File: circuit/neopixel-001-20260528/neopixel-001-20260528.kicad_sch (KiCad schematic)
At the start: 67 parts, among them J1 Conn_NeoPixel, J2 Conn_01x02_Pin, J3 Conn_01x02_Pin, P1 ESP32C3_{1}, P10 unitV3, P11 unitV4, P12 unitV4, P2 ESP32C3_{1}, P3 ESP32C3_{2}, P4 ESP32C3_{2}, P5 unitV1, P6 unitV1, P7 unitV2, P8 unitV2, P9 unitV3, SW1 SW_SPST_LED, SW2 SW_SPST_LED, SW3 SW_SPST_LED, SW4 SW_SPST_LED, U1 SSD1306, U2 Aexit_0-50_Voltmeter

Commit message: Update NeoPixel基板の回路図DRをした
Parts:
- J1: footprint Connector_FFC-FPC:JUSHUO_AFA07-S12FCA-00_1x12-1MP_P1.0mm_Horizontal -> (none)
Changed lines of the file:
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@@
 			)
 		)
-		(property "Footprint" "Connector_FFC-FPC:JUSHUO_AFA07-S12FCA-00_1x12-1MP_P1.0mm_Horizontal"
+		(property "Footprint" ""
 			(at 177.8 138.43 0)
 			(hide yes)

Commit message: Update ネオピクセル基板のフットプリント割り当てを進めた
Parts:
- J1: footprint (none) -> @Thrive_footprint_neopixel:AFC01-S12FCA-00
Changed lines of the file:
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@@
 			)
 		)
-		(property "Footprint" ""
+		(property "Footprint" "@Thrive_footprint_neopixel:AFC01-S12FCA-00"
 			(at 177.8 138.43 0)
 			(hide yes)

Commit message: Update ネオピク基板のPCBを進めてる。差動をどう配線すればいいんや
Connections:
- net P4_RX2-: now reaches P7.A10 (RX2-), P8.A10 (RX2-)
- net P4_RX2+: now reaches P7.A11 (RX2+), P8.A11 (RX2+)
- net P4_TX1+: now reaches P7.A2 (TX1+), P8.A2 (TX1+)
- net P4_TX1-: now reaches P7.A3 (TX1-), P8.A3 (TX1-)
- net P4_VBUS: now reaches P7.A4 (VBUS), P7.A9 (VBUS), P7.B4 (VBUS), P7.B9 (VBUS), P8.A4 (VBUS), P8.A9 (VBUS), P8.B4 (VBUS), P8.B9 (VBUS)
- net P4_CC: now reaches P7.A5 (CC), P8.A5 (CC)
- net P4_D-: now reaches P7.A6 (D+), P8.A6 (D+)
- net P4_D+: now reaches P7.A7 (D-), P8.A7 (D-)
- net P4_SBU1: now reaches P7.A8 (SBU1), P8.A8 (SBU1)
- net P4_RX1-: now reaches P7.B10 (RX1-), P8.B10 (RX1-)
- net P4_RX1+: now reaches P7.B11 (RX1+), P8.B11 (RX1+)
- net P4_TX2+: now reaches P7.B2 (TX2+), P8.B2 (TX2+)
- net P4_TX2-: now reaches P7.B3 (TX2-), P8.B3 (TX2-)
- net P4_VCONN: now reaches P7.B5 (VCONN), P8.B5 (VCONN)
- net P4_SBU2: now reaches P7.B8 (SBU2), P8.B8 (SBU2)
- net P6_RX2-: now reaches P11.A10 (RX2-), P12.A10 (RX2-)
- net P6_RX2+: now reaches P11.A11 (RX2+), P12.A11 (RX2+)
- net P6_TX1+: now reaches P11.A2 (TX1+), P12.A2 (TX1+)
- net P6_TX1-: now reaches P11.A3 (TX1-), P12.A3 (TX1-)
- net P6_VBUS: now reaches P11.A4 (VBUS), P11.A9 (VBUS), P11.B4 (VBUS), P11.B9 (VBUS), P12.A4 (VBUS), P12.A9 (VBUS), P12.B4 (VBUS), P12.B9 (VBUS)
- net P6_CC: now reaches P11.A5 (CC), P12.A5 (CC)
- net P6_D-: now reaches P11.A6 (D+), P12.A6 (D+)
- net P6_D+: now reaches P11.A7 (D-), P12.A7 (D-)
- net P6_SBU1: now reaches P11.A8 (SBU1), P12.A8 (SBU1)
- net P6_RX1-: now reaches P11.B10 (RX1-), P12.B10 (RX1-)
- net P6_RX1+: now reaches P11.B11 (RX1+), P12.B11 (RX1+)
- net P6_TX2+: now reaches P11.B2 (TX2+), P12.B2 (TX2+)
- net P6_TX2-: now reaches P11.B3 (TX2-), P12.B3 (TX2-)
- net P6_VCONN: now reaches P11.B5 (VCONN), P12.B5 (VCONN)
- net P6_SBU2: now reaches P11.B8 (SBU2), P12.B8 (SBU2)
- net P1_RX2-: now reaches P1.A10 (RX2-), P2.A10 (RX2-)
- net P1_RX2+: now reaches P1.A11 (RX2+), P2.A11 (RX2+)
- net P1_TX1+: now reaches P1.A2 (TX1+), P2.A2 (TX1+)
- net P1_TX1-: now reaches P1.A3 (TX1-), P2.A3 (TX1-)
- net P1_VBUS: now reaches P1.A4 (VBUS), P1.A9 (VBUS), P1.B4 (VBUS), P1.B9 (VBUS), P2.A4 (VBUS), P2.A9 (VBUS), P2.B4 (VBUS), P2.B9 (VBUS)
- net P1_CC: now reaches P1.A5 (CC), P2.A5 (CC)
- net P1_D-: now reaches P1.A6 (D+), P2.A6 (D+)
- net P1_D+: now reaches P1.A7 (D-), P2.A7 (D-)
- net P1_SBU1: now reaches P1.A8 (SBU1), P2.A8 (SBU1)
- net P1_RX1-: now reaches P1.B10 (RX1-), P2.B10 (RX1-)
- net P1_RX1+: now reaches P1.B11 (RX1+), P2.B11 (RX1+)
- net P1_TX2+: now reaches P1.B2 (TX2+), P2.B2 (TX2+)
- net P1_TX2-: now reaches P1.B3 (TX2-), P2.B3 (TX2-)
- net P1_VCONN: now reaches P1.B5 (VCONN), P2.B5 (VCONN)
- net P1_SBU2: now reaches P1.B8 (SBU2), P2.B8 (SBU2)
- net P3_RX2-: now reaches P5.A10 (RX2-), P6.A10 (RX2-)
- net P3_RX2+: now reaches P5.A11 (RX2+), P6.A11 (RX2+)
- net P3_TX1+: now reaches P5.A2 (TX1+), P6.A2 (TX1+)
- net P3_TX1-: now reaches P5.A3 (TX1-), P6.A3 (TX1-)
- net P3_VBUS: now reaches P5.A4 (VBUS), P5.A9 (VBUS), P5.B4 (VBUS), P5.B9 (VBUS), P6.A4 (VBUS), P6.A9 (VBUS), P6.B4 (VBUS), P6.B9 (VBUS)
- net P3_CC: now reaches P5.A5 (CC), P6.A5 (CC)
- net P3_D-: now reaches P5.A6 (D+), P6.A6 (D+)
- net P3_D+: now reaches P5.A7 (D-), P6.A7 (D-)
- net P3_SBU1: now reaches P5.A8 (SBU1), P6.A8 (SBU1)
- net P3_RX1-: now reaches P5.B10 (RX1-), P6.B10 (RX1-)
- net P3_RX1+: now reaches P5.B11 (RX1+), P6.B11 (RX1+)
- net P3_TX2+: now reaches P5.B2 (TX2+), P6.B2 (TX2+)
- net P3_TX2-: now reaches P5.B3 (TX2-), P6.B3 (TX2-)
- net P3_VCONN: now reaches P5.B5 (VCONN), P6.B5 (VCONN)
- net P3_SBU2: now reaches P5.B8 (SBU2), P6.B8 (SBU2)
- net P2_RX2-: now reaches P3.A10 (RX2-), P4.A10 (RX2-)
- net P2_RX2+: now reaches P3.A11 (RX2+), P4.A11 (RX2+)
- net P2_TX1+: now reaches P3.A2 (TX1+), P4.A2 (TX1+)
- net P2_TX1-: now reaches P3.A3 (TX1-), P4.A3 (TX1-)
- net P2_VBUS: now reaches P3.A4 (VBUS), P3.A9 (VBUS), P3.B4 (VBUS), P3.B9 (VBUS), P4.A4 (VBUS), P4.A9 (VBUS), P4.B4 (VBUS), P4.B9 (VBUS)
- net P2_CC: now reaches P3.A5 (CC), P4.A5 (CC)
- net P2_D-: now reaches P3.A6 (D+), P4.A6 (D+)
- net P2_D+: now reaches P3.A7 (D-), P4.A7 (D-)
- net P2_SBU1: now reaches P3.A8 (SBU1), P4.A8 (SBU1)
- net P2_RX1-: now reaches P3.B10 (RX1-), P4.B10 (RX1-)
- net P2_RX1+: now reaches P3.B11 (RX1+), P4.B11 (RX1+)
- net P2_TX2+: now reaches P3.B2 (TX2+), P4.B2 (TX2+)
- net P2_TX2-: now reaches P3.B3 (TX2-), P4.B3 (TX2-)
- net P2_VCONN: now reaches P3.B5 (VCONN), P4.B5 (VCONN)
- net P2_SBU2: now reaches P3.B8 (SBU2), P4.B8 (SBU2)
- net P5_RX2-: now reaches P10.A10 (RX2-), P9.A10 (RX2-)
- net P5_RX2+: now reaches P10.A11 (RX2+), P9.A11 (RX2+)
- net P5_TX1+: now reaches P10.A2 (TX1+), P9.A2 (TX1+)
- net P5_TX1-: now reaches P10.A3 (TX1-), P9.A3 (TX1-)
- net P5_VBUS: now reaches P10.A4 (VBUS), P10.A9 (VBUS), P10.B4 (VBUS), P10.B9 (VBUS), P9.A4 (VBUS), P9.A9 (VBUS), P9.B4 (VBUS), P9.B9 (VBUS)
- net P5_CC: now reaches P10.A5 (CC), P9.A5 (CC)
- net P5_D-: now reaches P10.A6 (D+), P9.A6 (D+)
- net P5_D+: now reaches P10.A7 (D-), P9.A7 (D-)
- net P5_SBU1: now reaches P10.A8 (SBU1), P9.A8 (SBU1)
- net P5_RX1-: now reaches P10.B10 (RX1-), P9.B10 (RX1-)
- net P5_RX1+: now reaches P10.B11 (RX1+), P9.B11 (RX1+)
- net P5_TX2+: now reaches P10.B2 (TX2+), P9.B2 (TX2+)
- net P5_TX2-: now reaches P10.B3 (TX2-), P9.B3 (TX2-)
- net P5_VCONN: now reaches P10.B5 (VCONN), P9.B5 (VCONN)
- net P5_SBU2: now reaches P10.B8 (SBU2), P9.B8 (SBU2)
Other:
- moved on the sheet: C1, C10, C11, C12, C13, C14, C15, C16, C17, C18, C19, C2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

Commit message: Update ネオピクセル基板のコンポーネントコンポーネント再度仮配置。時間返せ
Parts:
- P10, P12, P2, P4, P6, P8: footprint @Thrive_footprint_neopixel:USB_Type-C_Vertical_ C6332304 -> Connector_USB:USB_C_Receptacle_GCT_USB4105-xx-A_16P_TopMnt_Horizontal
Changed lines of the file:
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@@
 			)
 		)
-		(property "Footprint" "@Thrive_footprint_neopixel:USB_Type-C_Vertical_ C6332304"
+		(property "Footprint" "Connector_USB:USB_C_Receptacle_GCT_USB4105-xx-A_16P_TopMnt_Horizontal"
 			(at 191.77 142.24 0)
 			(hide yes)
@@
 			)
 		)
-		(property "Footprint" "@Thrive_footprint_neopixel:USB_Type-C_Vertical_ C6332304"
+		(property "Footprint" "Connector_USB:USB_C_Receptacle_GCT_USB4105-xx-A_16P_TopMnt_Horizontal"
 			(at 92.71 142.24 0)
 			(hide yes)
@@
 			)
 		)
-		(property "Footprint" "@Thrive_footprint_neopixel:USB_Type-C_Vertical_ C6332304"
+		(property "Footprint" "Connector_USB:USB_C_Receptacle_GCT_USB4105-xx-A_16P_TopMnt_Horizontal"
 			(at 191.77 232.41 0)
 			(hide yes)
@@
 			)
 		)
-		(property "Footprint" "@Thrive_footprint_neopixel:USB_Type-C_Vertical_ C6332304"
+		(property "Footprint" "Connector_USB:USB_C_Receptacle_GCT_USB4105-xx-A_16P_TopMnt_Horizontal"
 			(at 92.71 232.41 0)
 			(hide yes)
@@
 			)
 		)
-		(property "Footprint" "@Thrive_footprint_neopixel:USB_Type-C_Vertical_ C6332304"
+		(property "Footprint" "Connector_USB:USB_C_Receptacle_GCT_USB4105-xx-A_16P_TopMnt_Horizontal"
 			(at 92.71 52.07 0)
 			(hide yes)
@@
 			)
 		)
-		(property "Footprint" "@Thrive_footprint_neopixel:USB_Type-C_Vertical_ C6332304"
+		(property "Footprint" "Connector_USB:USB_C_Receptacle_GCT_USB4105-xx-A_16P_TopMnt_Horizontal"
 			(at 191.77 52.07 0)
 			(hide yes)

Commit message: Update ネオピクセル基板のコンポーネントを再配置した。明日配線する。もう今日か
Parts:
- P10, P12, P2, P4, P6, P8: footprint Connector_USB:USB_C_Receptacle_GCT_USB4105-xx-A_16P_TopMnt_Horizontal -> @Thrive_footprint_neopixel:USB_Type-C_Vertical_ C6332304
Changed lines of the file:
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@@
 			)
 		)
-		(property "Footprint" "Connector_USB:USB_C_Receptacle_GCT_USB4105-xx-A_16P_TopMnt_Horizontal"
+		(property "Footprint" "@Thrive_footprint_neopixel:USB_Type-C_Vertical_ C6332304"
 			(at 191.77 142.24 0)
 			(hide yes)
@@
 			)
 		)
-		(property "Footprint" "Connector_USB:USB_C_Receptacle_GCT_USB4105-xx-A_16P_TopMnt_Horizontal"
+		(property "Footprint" "@Thrive_footprint_neopixel:USB_Type-C_Vertical_ C6332304"
 			(at 92.71 142.24 0)
 			(hide yes)
@@
 			)
 		)
-		(property "Footprint" "Connector_USB:USB_C_Receptacle_GCT_USB4105-xx-A_16P_TopMnt_Horizontal"
+		(property "Footprint" "@Thrive_footprint_neopixel:USB_Type-C_Vertical_ C6332304"
 			(at 191.77 232.41 0)
 			(hide yes)
@@
 			)
 		)
-		(property "Footprint" "Connector_USB:USB_C_Receptacle_GCT_USB4105-xx-A_16P_TopMnt_Horizontal"
+		(property "Footprint" "@Thrive_footprint_neopixel:USB_Type-C_Vertical_ C6332304"
 			(at 92.71 232.41 0)
 			(hide yes)
@@
 			)
 		)
-		(property "Footprint" "Connector_USB:USB_C_Receptacle_GCT_USB4105-xx-A_16P_TopMnt_Horizontal"
+		(property "Footprint" "@Thrive_footprint_neopixel:USB_Type-C_Vertical_ C6332304"
 			(at 92.71 52.07 0)
 			(hide yes)
@@
 			)
 		)
-		(property "Footprint" "Connector_USB:USB_C_Receptacle_GCT_USB4105-xx-A_16P_TopMnt_Horizontal"
+		(property "Footprint" "@Thrive_footprint_neopixel:USB_Type-C_Vertical_ C6332304"
 			(at 191.77 52.07 0)
 			(hide yes)

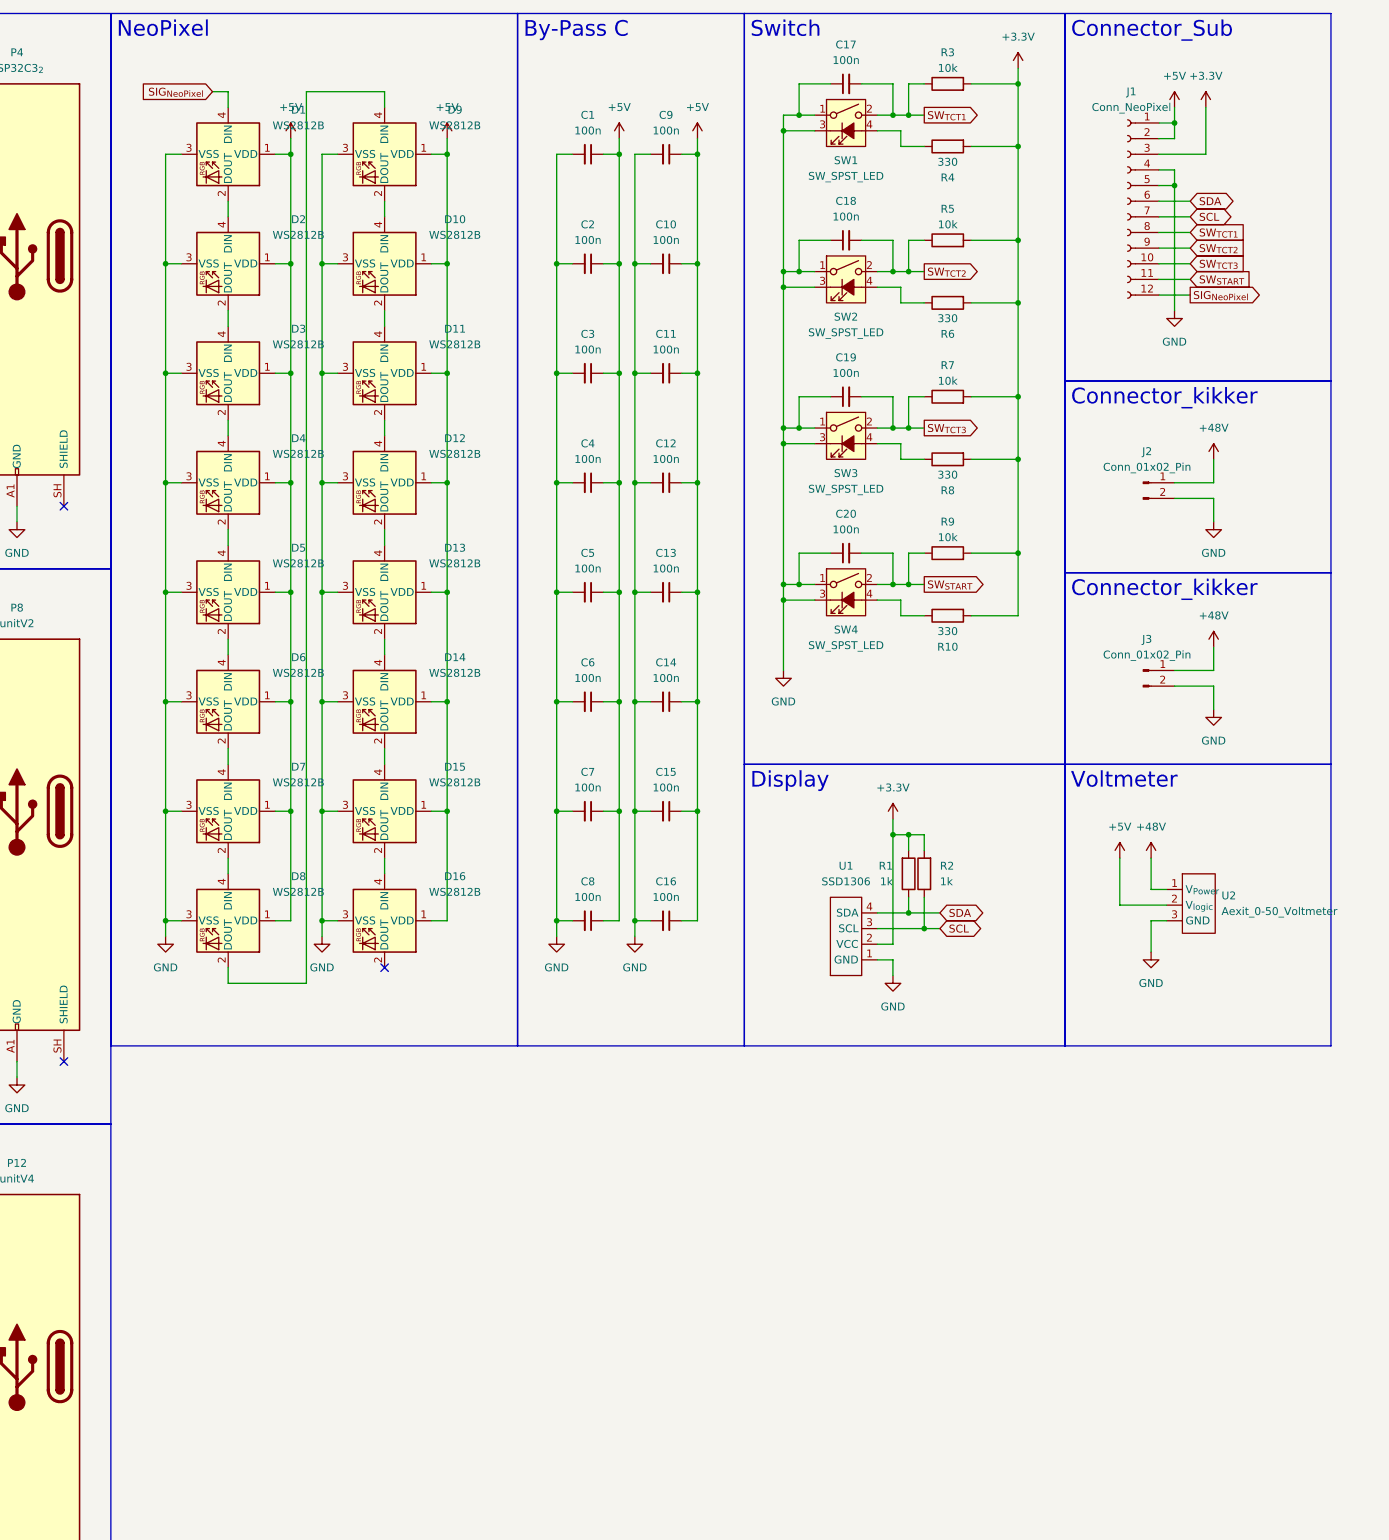
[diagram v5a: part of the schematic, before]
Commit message: Update ネオピクセル基板のTCTSW周りを更新
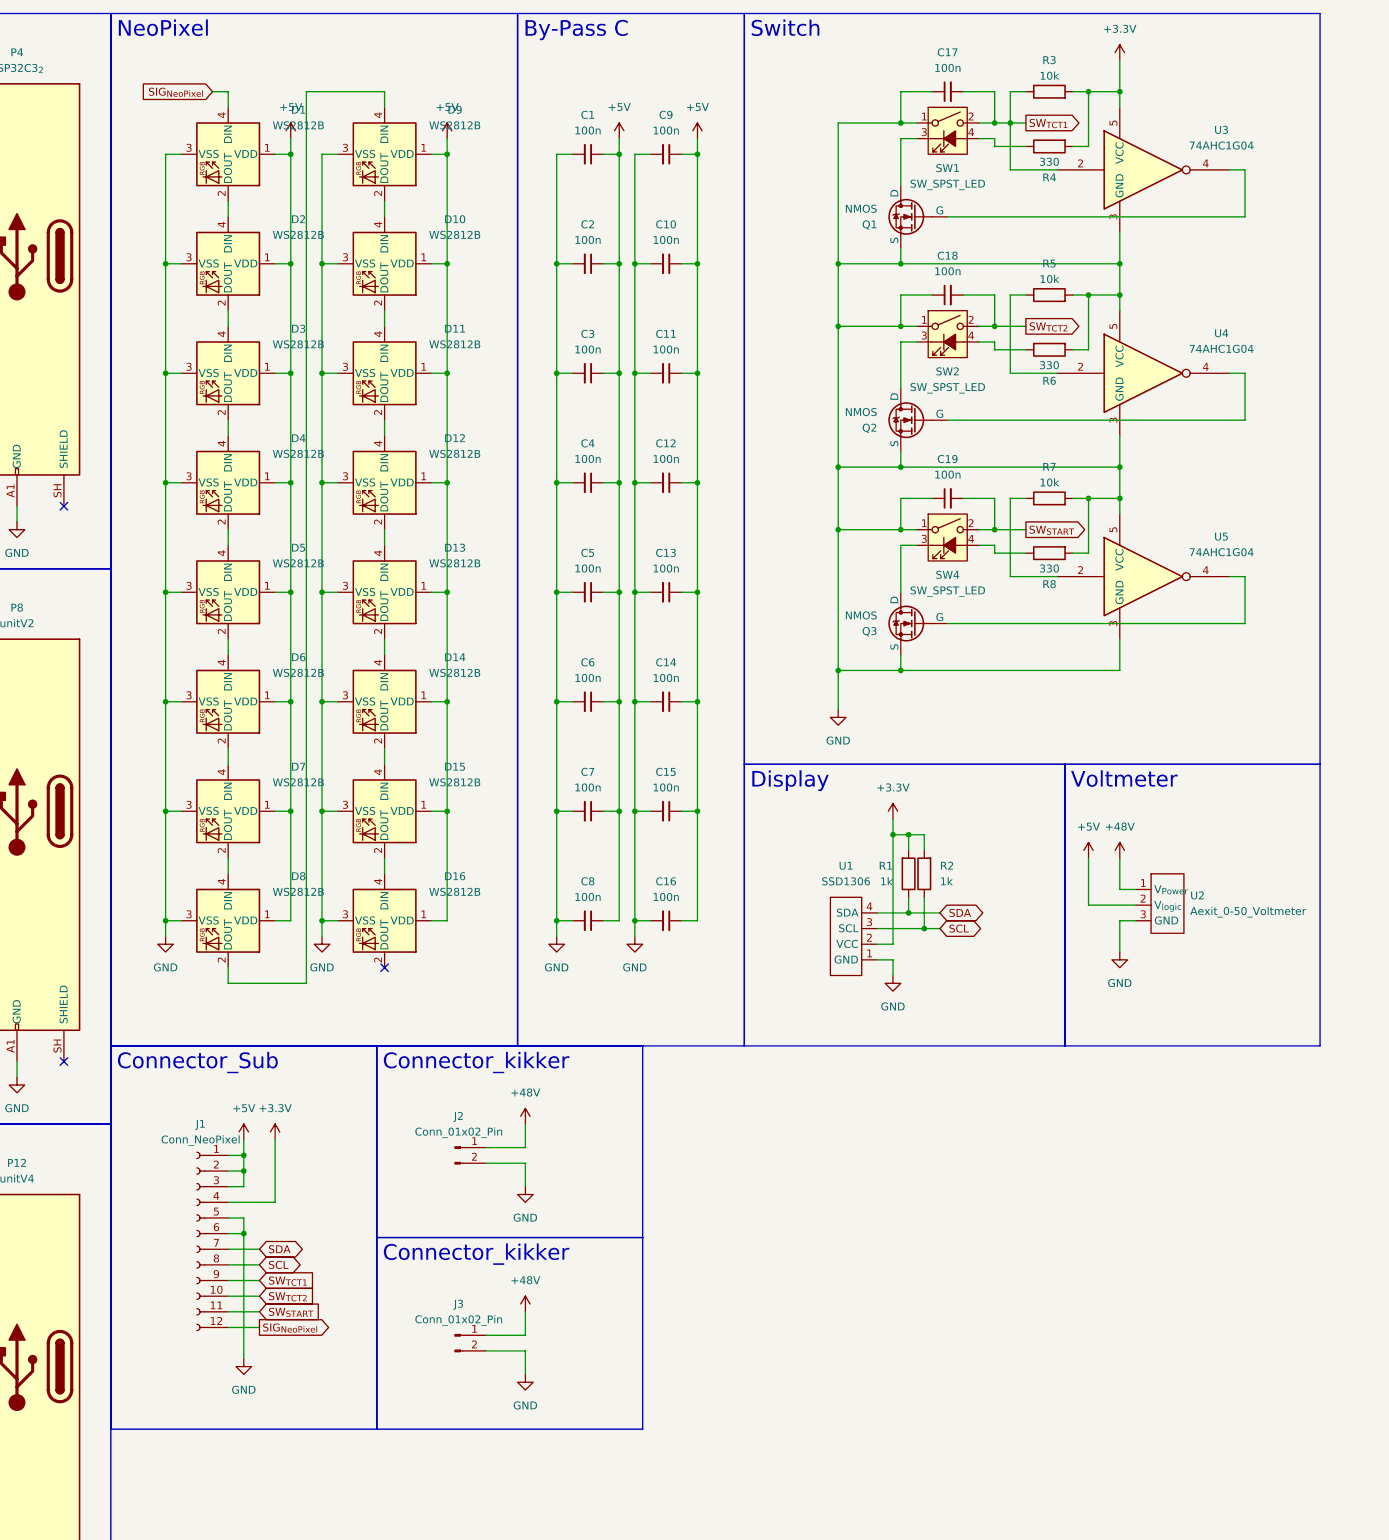
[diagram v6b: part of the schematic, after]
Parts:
- removed C20: 100n, Capacitor_SMD:C_0805_2012Metric, symbol Device:C_Small
- removed R10: 330, Resistor_SMD:R_0805_2012Metric, symbol Device:R
- removed R9: 10k, Resistor_SMD:R_0805_2012Metric, symbol Device:R
- removed SW3: SW_SPST_LED, @Thrive_footprint_neopixel:ST-12-401FC-G, symbol Switch:SW_SPST_LED
- added Q1, Q2, Q3: NMOS, symbol Simulation_SPICE:NMOS
- added U3, U4, U5: 74AHC1G04, symbol 74xGxx:74AHC1G04
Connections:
- net +3.3V: now also J1.4 (Pin_4), U3.5 (VCC); no longer J1.3 (Pin_3), R5.2, R6.2, R7.2, R8.2
- net +5V: now also J1.3 (Pin_3)
- net GND: now also J1.6 (Pin_6), R5.2, R6.2, R7.2, R8.2, Q1.3 (S), Q2.3 (S), Q3.3 (S), U3.3 (GND), U4.3 (GND), U4.5 (VCC), U5.3 (GND), U5.5 (VCC); no longer J1.4 (Pin_4), SW1.3 (K), SW2.3 (K), SW4.3 (K)
- net SCL: now also J1.8 (Pin_8); no longer J1.7 (Pin_7)
- net SDA: now also J1.7 (Pin_7); no longer J1.6 (Pin_6)
- net SW_{START}: now also C19.2
- net SW_{TCT1}: now also J1.9 (Pin_9), U3.2; no longer J1.8 (Pin_8)
- net SW_{TCT2}: now also J1.10 (Pin_10); no longer J1.9 (Pin_9), R5.1
- net at R8.1: now also SW4.4 (A)
- removed net SW_{TCT3}: C19.2, J1.10 (Pin_10), R7.1
- new net: Q1.2 (G), U3.4
- new net: R5.1, U4.2
- new net: Q2.2 (G), U4.4
- new net: Q2.1 (D), SW2.3 (K)
- new net: R7.1, U5.2
- new net: Q3.2 (G), U5.4
- new net: Q1.1 (D), SW1.3 (K)
- new net: Q3.1 (D), SW4.3 (K)
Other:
- moved on the sheet: C17, C18, C19, J1, J2, J3, R3, R4, R5, R6, R7, R8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

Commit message: Update ネオピクセル基板のPCBを進めた。タクトスイッチだけ怪しい
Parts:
- added R10, R9: 500, Resistor_SMD:R_0805_2012Metric, symbol Device:R_Small
- Q1, Q2, Q3: footprint (none) -> Package_TO_SOT_SMD:TSOT-23
- U3, U4, U5: footprint (none) -> Package_TO_SOT_SMD:SOT-23-5_HandSoldering
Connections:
- net +3.3V: now also R5.2, R6.2, R7.2, R8.2, U4.5 (VCC), U5.5 (VCC)
- net GND: now also R10.2; no longer R5.2, R6.2, R7.2, R8.2, U4.5 (VCC), U5.5 (VCC)
- net SIG_{NeoPixel}: now also R9.1; no longer D1.4 (DIN)
- net SW_{START}: now also R7.1, U5.2
- net SW_{TCT2}: now also R5.1, U4.2
- net at D16.2 (DOUT): now also R10.1
- new net: D1.4 (DIN), R9.2
- no-connect marks 13 -> 12

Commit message: Update ネオピクセル基板のシルクスクリーンを整えた
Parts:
- J1: value Conn_NeoPixel -> Conn_Sub
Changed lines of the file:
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@@
 			)
 		)
-		(property "Value" "Conn_NeoPixel"
+		(property "Value" "Conn_Sub"
 			(at 225.425 195.58 0)
 			(show_name no)
